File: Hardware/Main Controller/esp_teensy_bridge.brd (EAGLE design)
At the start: 99.8 x 88.1 mm, 64 parts, among them IC1 BQ79600PWRQ1, Q5 VISHAY_SIS862DN-T1-GE3VISHAY_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, Q6 VISHAY_SIS862DN-T1-GE3VISHAY_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, Q7 VISHAY_SIS862DN-T1-GE3VISHAY_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, Q8 VISHAY_SIS862DN-T1-GE3VISHAY_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, X1 5566-12

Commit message: Fixed LED issue
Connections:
- net CONTACTORN_CTRL: now also R14.1
- net CONTACTORPRECHARGE_CTRL: now also R12.1
- net CONTACTORP_CTRL: now also R13.1
- net COOLANT_CTRL: now also R11.1
- net N$12: no longer R12.1
- net N$2: no longer R13.1
- net N$5: no longer R14.1
- net N$6: no longer R11.1
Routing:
- net COOLANT_CTRL: track 36.6 -> 40.7 mm
- net CONTACTORPRECHARGE_CTRL: track 26.1 -> 30.2 mm
- net CONTACTORP_CTRL: track 15.9 -> 19.9 mm
- net CONTACTORN_CTRL: track 11.0 -> 15.0 mm
- net N$6: track 15.3 -> 12.0 mm
- net N$5: track 15.3 -> 12.0 mm
- net N$2: track 16.7 -> 13.4 mm
- net N$12: track 16.7 -> 13.4 mm
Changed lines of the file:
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@@
 <wire x1="9.945" y1="68.58" x2="9.995" y2="68.63" width="0.3048" layer="1"/>
 <wire x1="9.995" y1="68.63" x2="9.995" y2="71.4" width="0.3048" layer="1"/>
+<contactref element="R14" pad="1"/>
+<wire x1="9.1952" y1="71.73125" x2="9.1952" y2="71.9823" width="0.3048" layer="1"/>
+<wire x1="9.1952" y1="71.9823" x2="7.2" y2="73.9775" width="0.3048" layer="1"/>
+<wire x1="9.995" y1="71.4" x2="9.52645" y2="71.4" width="0.3048" layer="1"/>
+<wire x1="9.52645" y1="71.4" x2="9.1952" y2="71.73125" width="0.3048" layer="1"/>
 </signal>
 <signal name="N$5">
 <contactref element="CONTACTOR_N" pad="2"/>
-<contactref element="R14" pad="1"/>
 <contactref element="Q5" pad="5,6,7,8-2"/>
 <contactref element="Q5" pad="5,6,7,8-5"/>
@@
 <wire x1="10.7948" y1="73.5822" x2="10.7948" y2="73.70875" width="0.3048" layer="1"/>
 <wire x1="10.7948" y1="73.70875" x2="10.52605" y2="73.9775" width="0.3048" layer="1"/>
-<wire x1="10.52605" y1="73.9775" x2="7.2" y2="73.9775" width="0.3048" layer="1"/>
 <wire x1="12.98" y1="72.06" x2="12.98" y2="72.72" width="0.3048" layer="1"/>
 <wire x1="11.987" y1="72.39" x2="12.65" y2="72.39" width="0.3048" layer="1"/>
@@
 <signal name="N$2">
 <contactref element="CONTACTOR_P" pad="2"/>
-<contactref element="R13" pad="1"/>
 <contactref element="Q6" pad="5,6,7,8-2"/>
 <contactref element="Q6" pad="5,6,7,8-5"/>
@@
 <wire x1="23.4948" y1="73.5822" x2="23.4948" y2="73.70875" width="0.3048" layer="1"/>
 <wire x1="23.4948" y1="73.70875" x2="23.22605" y2="73.9775" width="0.3048" layer="1"/>
-<wire x1="23.22605" y1="73.9775" x2="19.9" y2="73.9775" width="0.3048" layer="1"/>
 <wire x1="25.68" y1="72.06" x2="25.68" y2="72.72" width="0.3048" layer="1"/>
 <wire x1="25.68" y1="72.06" x2="25.35" y2="72.39" width="0.3048" layer="1"/>
@@
 <wire x1="22.645" y1="68.58" x2="22.695" y2="68.63" width="0.3048" layer="1"/>
 <wire x1="22.695" y1="68.63" x2="22.695" y2="71.4" width="0.3048" layer="1"/>
+<contactref element="R13" pad="1"/>
+<wire x1="21.8952" y1="71.73125" x2="21.8952" y2="71.9823" width="0.3048" layer="1"/>
+<wire x1="21.8952" y1="71.9823" x2="19.9" y2="73.9775" width="0.3048" layer="1"/>
+<wire x1="22.695" y1="71.4" x2="22.22645" y2="71.4" width="0.3048" layer="1"/>
+<wire x1="22.22645" y1="71.4" x2="21.8952" y2="71.73125" width="0.3048" layer="1"/>
 </signal>
 <signal name="CONTACTORPRECHARGE_CTRL">
@@
 <wire x1="35.345" y1="68.58" x2="25.82605" y2="68.58" width="0.3048" layer="1"/>
 <contactref element="Q7" pad="4"/>
-<wire x1="35.345" y1="68.58" x2="35.345" y2="71.35" width="0.3048" layer="1"/>
+<wire x1="35.345" y1="68.58" x2="35.345" y2="71.12" width="0.3048" layer="1"/>
+<wire x1="35.345" y1="71.12" x2="35.345" y2="71.35" width="0.3048" layer="1"/>
 <wire x1="35.345" y1="71.35" x2="35.395" y2="71.4" width="0.3048" layer="1"/>
+<contactref element="R12" pad="1"/>
+<wire x1="32.6" y1="73.9775" x2="34.5952" y2="71.9823" width="0.3048" layer="1"/>
+<wire x1="34.5952" y1="71.9823" x2="34.5952" y2="71.73125" width="0.3048" layer="1"/>
+<wire x1="34.5952" y1="71.73125" x2="34.77375" y2="71.5527" width="0.3048" layer="1"/>
+<wire x1="34.77375" y1="71.5527" x2="34.9123" y2="71.5527" width="0.3048" layer="1"/>
+<wire x1="34.9123" y1="71.5527" x2="35.345" y2="71.12" width="0.3048" layer="1"/>
 </signal>
 <signal name="N$12">
 <contactref element="CONTACTOR_PRECHARGE" pad="2"/>
-<contactref element="R12" pad="1"/>
 <contactref element="Q7" pad="5,6,7,8-2"/>
 <contactref element="Q7" pad="5,6,7,8-5"/>
@@
 <wire x1="36.1948" y1="73.5822" x2="36.1948" y2="73.70875" width="0.3048" layer="1"/>
 <wire x1="36.1948" y1="73.70875" x2="35.92605" y2="73.9775" width="0.3048" layer="1"/>
-<wire x1="35.92605" y1="73.9775" x2="32.6" y2="73.9775" width="0.3048" layer="1"/>
 <wire x1="38.38" y1="72.06" x2="38.05" y2="72.39" width="0.3048" layer="1"/>
 <wire x1="38.05" y1="72.39" x2="37.387" y2="72.39" width="0.3048" layer="1"/>
@@
 <signal name="N$6">
 <contactref element="COOLANT-1" pad="2"/>
-<contactref element="R11" pad="1"/>
 <contactref element="Q8" pad="5,6,7,8-2"/>
 <contactref element="Q8" pad="5,6,7,8-5"/>
@@
 <wire x1="48.8948" y1="73.5822" x2="48.8948" y2="73.70875" width="0.3048" layer="1"/>
 <wire x1="48.8948" y1="73.70875" x2="48.62605" y2="73.9775" width="0.3048" layer="1"/>
-<wire x1="48.62605" y1="73.9775" x2="45.3" y2="73.9775" width="0.3048" layer="1"/>
 <wire x1="51.08" y1="72.06" x2="51.08" y2="72.72" width="0.3048" layer="1"/>
 <wire x1="51.08" y1="72.06" x2="50.75" y2="72.39" width="0.3048" layer="1"/>
@@
 <contactref element="Q8" pad="4"/>
 <wire x1="48.045" y1="68.58" x2="48.095" y2="68.63" width="0.3048" layer="1"/>
-<wire x1="48.095" y1="68.63" x2="48.095" y2="71.4" width="0.3048" layer="1"/>
+<wire x1="48.095" y1="68.63" x2="48.095" y2="71.12" width="0.3048" layer="1"/>
+<contactref element="R11" pad="1"/>
+<wire x1="48.095" y1="71.12" x2="48.095" y2="71.4" width="0.3048" layer="1"/>
+<wire x1="45.3" y1="73.9775" x2="47.2952" y2="71.9823" width="0.3048" layer="1"/>
+<wire x1="47.2952" y1="71.9823" x2="47.2952" y2="71.73125" width="0.3048" layer="1"/>
+<wire x1="47.2952" y1="71.73125" x2="47.47375" y2="71.5527" width="0.3048" layer="1"/>
+<wire x1="47.47375" y1="71.5527" x2="47.6623" y2="71.5527" width="0.3048" layer="1"/>
+<wire x1="47.6623" y1="71.5527" x2="48.095" y2="71.12" width="0.3048" layer="1"/>
 </signal>
 <signal name="N$7">

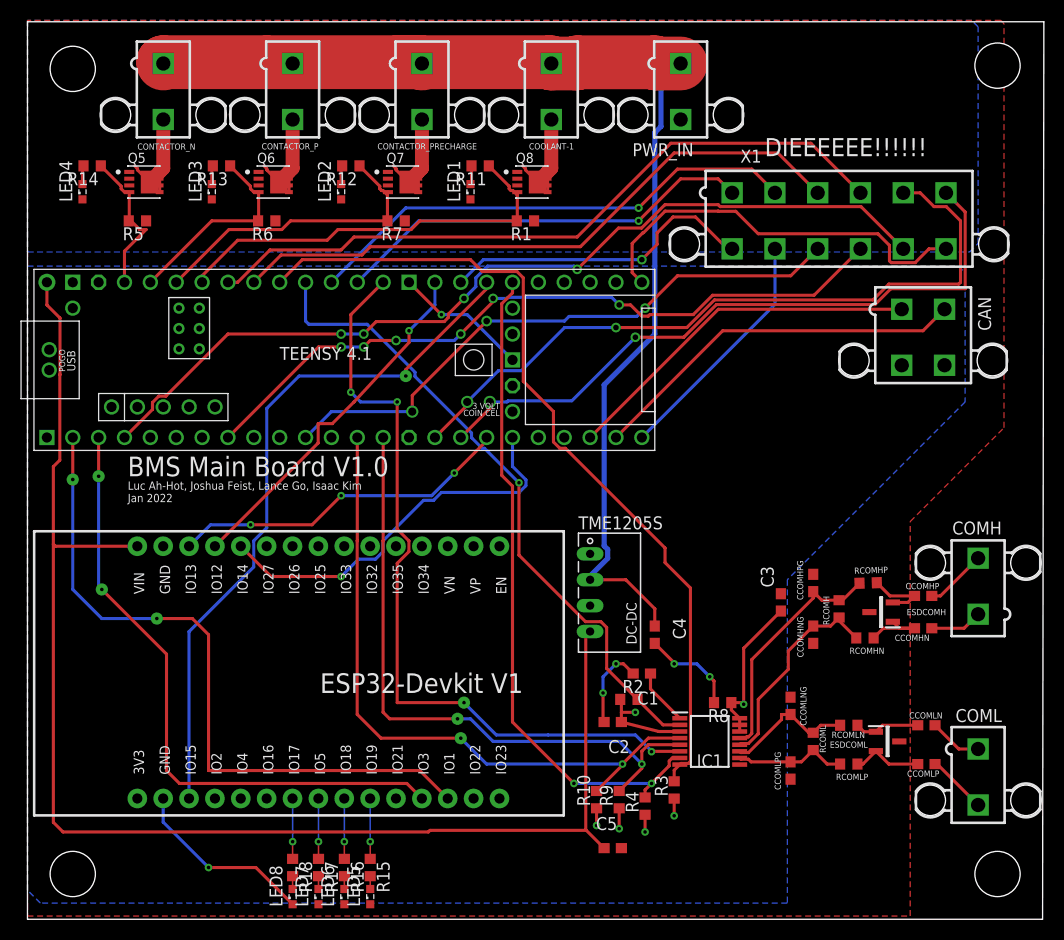
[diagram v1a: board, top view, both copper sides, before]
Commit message: Fixed LED VCC and resistors, coolant is now PWM, CAN transceiver added, removed unnecessary resistor
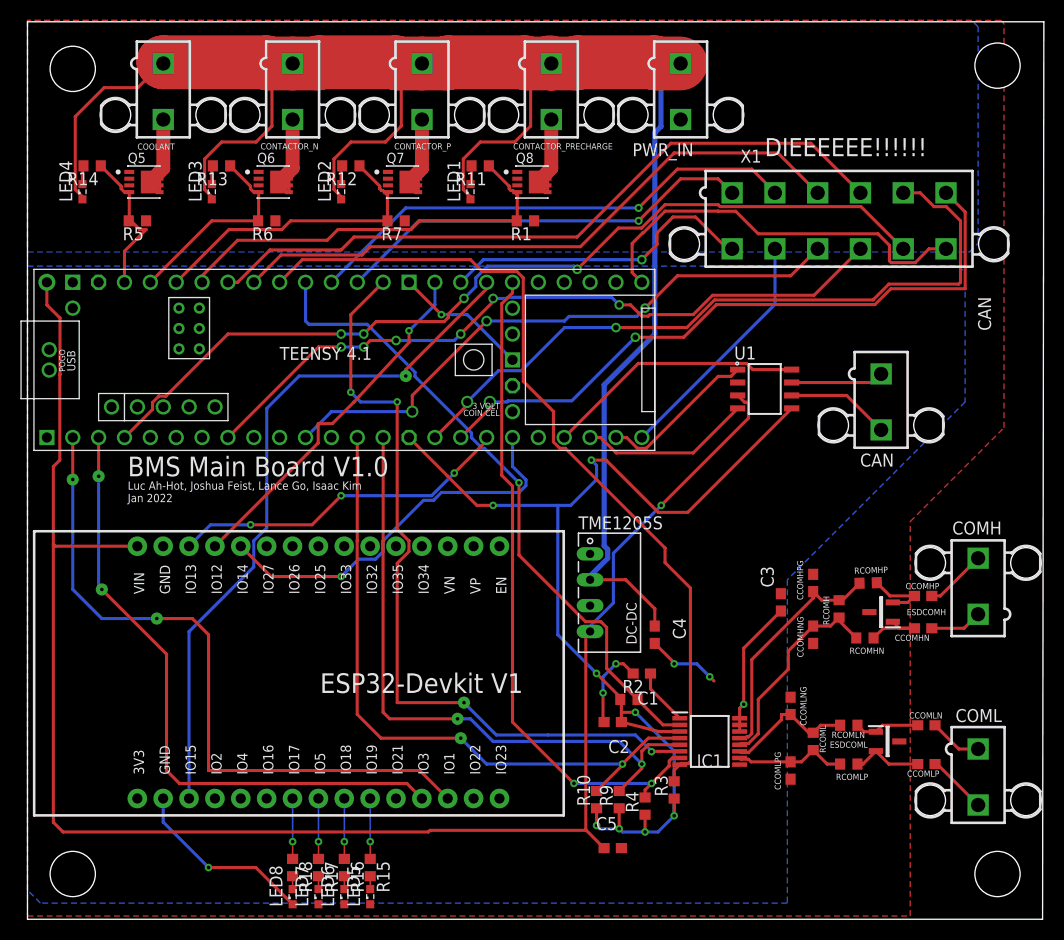
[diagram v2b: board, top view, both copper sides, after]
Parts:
- removed CAN1: 5566-4, con-molex:5566-4
- removed COOLANT-1: 5566-2, con-molex:5566-2
- removed R8: 100k, rcl:R0603
- added CAN, COOLANT: 5566-2, con-molex:5566-2
- added U1: MCP2562-E/SN, MCP2562-E_SN:SOIC127P600X175-8N
- R11, R12, R13, R14: value 100k -> 10k
- moved CONTACTOR_PRECHARGE 12.7 mm to (51.4, 81.3)
- moved CONTACTOR_N 12.7 mm to (26.0, 81.3)
- moved CONTACTOR_P 12.7 mm to (38.7, 81.3)
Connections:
- removed net N$7: CAN1.1, U$3.30-CRX3
- removed net N$8: CAN1.2, U$3.31-CTX3
- removed net NCS/CS: U$3.10-CS\MQSR
- new net 3V3: C2.1, IC1.3, R10.1, R2.1, R3.1, R4.1, R9.1, U$3.3V3-1, U1.5
- new net CANH: CAN.1, U1.7
- new net CANL: CAN.2, U1.6
- new net CRX: U$3.30-CRX3, U1.4
- new net CSTBY: U$3.29-TX7, U1.8
- new net CTX: U$3.31-CTX3, U1.1
- net 5V: now also U1.3; no longer C2.1, IC1.3, R10.1, R2.1, R3.1, R4.1, R8.1, R9.1
- net CONTACTORN_CTRL: now also Q6.4, R13.1, R6.2, U$3.22-A8/CTX1; no longer Q5.4, R14.1, R5.2, U$3.23-A9/CRX1/MCLK1
- net CONTACTORPRECHARGE_CTRL: now also Q8.4, R1.2, R11.1, U$3.20-A6/TX5/LRCLK1; no longer Q7.4, R12.1, R7.2, U$3.21-A7/RX5/BCLK1
- net CONTACTORP_CTRL: now also Q7.4, R12.1, R7.2, U$3.21-A7/RX5/BCLK1; no longer Q6.4, R13.1, R6.2, U$3.22-A8/CTX1
- net COOLANT_CTRL: now also Q5.4, R14.1, R5.2, U$3.23-A9/CRX1/MCLK1; no longer Q8.4, R1.2, R11.1, U$3.20-A6/TX5/LRCLK1
- net GND: now also U1.2; no longer CAN1.3, LED1.C, LED2.C, LED3.C, LED4.C, R8.2
- net N$12: now also CONTACTOR_P.2; no longer CONTACTOR_PRECHARGE.2
- net N$2: now also CONTACTOR_N.2; no longer CONTACTOR_P.2
- net N$5: now also COOLANT.2; no longer CONTACTOR_N.2
- net N$6: now also CONTACTOR_PRECHARGE.2; no longer COOLANT-1.2
- net VCC: now also COOLANT.1, LED1.C, LED2.C, LED3.C, LED4.C; no longer COOLANT-1.1
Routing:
- net 3V3: track 0.00 -> 108.8 mm, vias 0 -> 8
- net VCC: track 117.2 -> 192.1 mm
- net N$8: track 37.5 -> 0.00 mm
- net N$7: track 35.8 -> 0.00 mm
- net COOLANT_CTRL: track 40.7 -> 15.0 mm
- net CSTBY: track 0.00 -> 25.6 mm
- net CRX: track 0.00 -> 16.9 mm
- net CTX: track 0.00 -> 15.6 mm
- net 5V: track 168.8 -> 180.8 mm, vias 6 -> 2
- net CONTACTORPRECHARGE_CTRL: track 30.2 -> 40.7 mm
- net CONTACTORP_CTRL: track 19.9 -> 30.2 mm
- net CANL: track 0.00 -> 10.2 mm
- net CANH: track 0.00 -> 9.13 mm
- net CONTACTORN_CTRL: track 15.0 -> 19.9 mm
- net N$6: track 12.0 -> 9.81 mm
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
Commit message: Work on BQ library, RC fix for SR
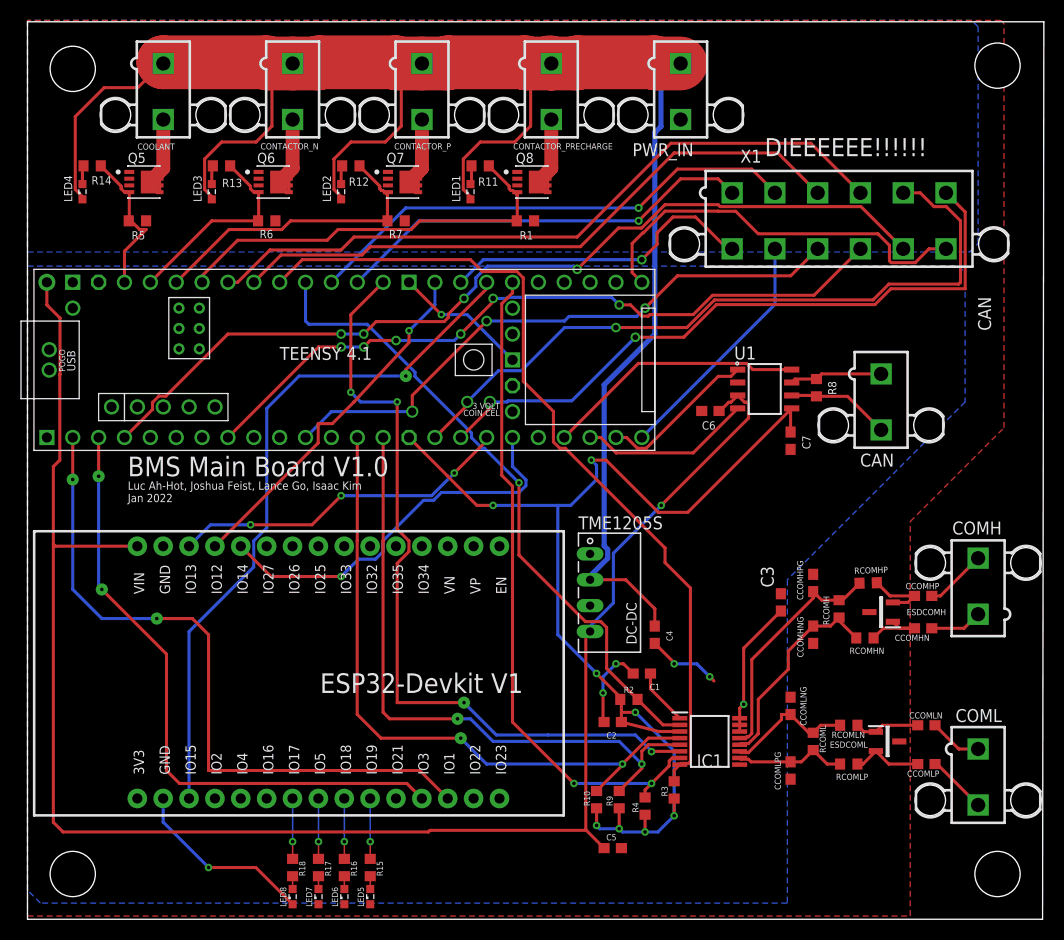
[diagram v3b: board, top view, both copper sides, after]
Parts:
- added C6, C7: 0.1μF, rcl:C0603
- added R8: 120, rcl:R0603
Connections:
- net 3V3: now also C7.1
- net 5V: now also C6.1
- net CANH: now also R8.1
- net CANL: now also R8.2
- net GND: now also C6.2, C7.2
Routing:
- net 5V: track 180.8 -> 183.3 mm
- net 3V3: track 108.8 -> 111.2 mm

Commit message: ESP32-devkitc-32D instead ov DEVKIT V1
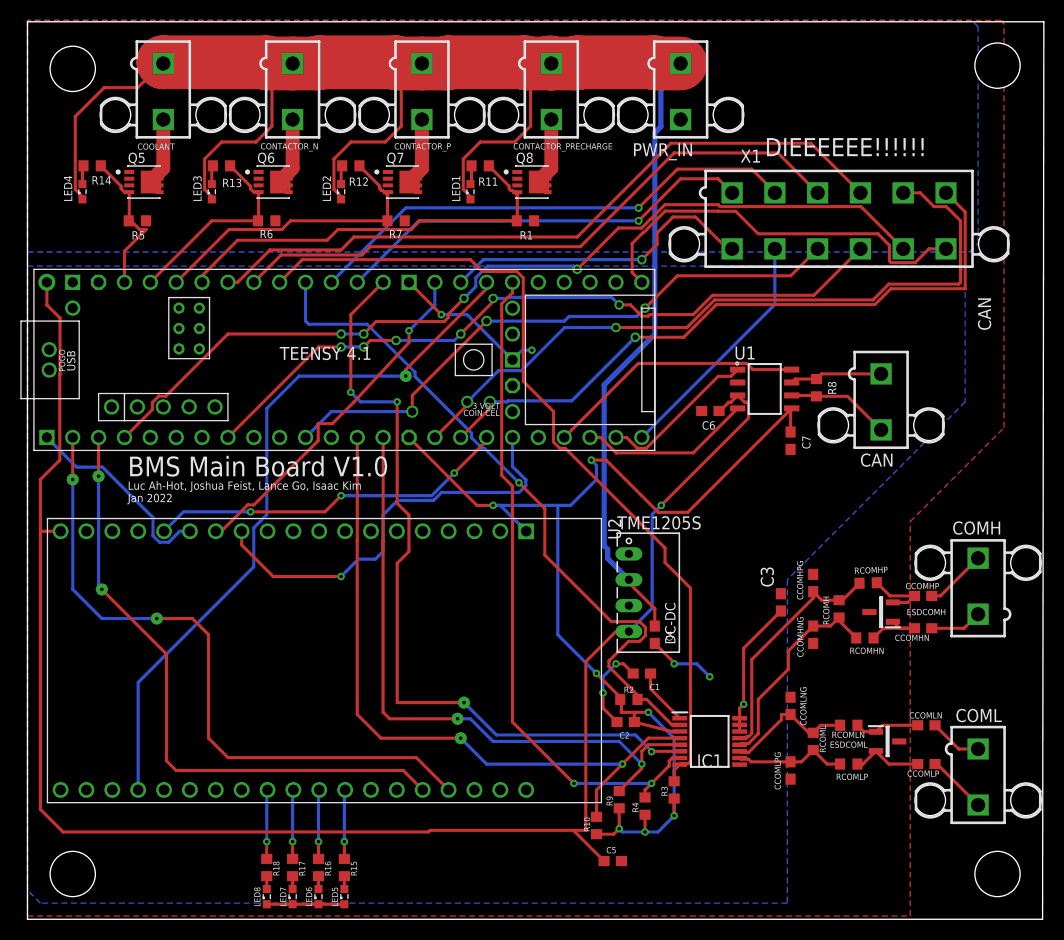
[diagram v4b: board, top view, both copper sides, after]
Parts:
- removed U$2: ESP32DEVKITV1, ESP32-DEVKITV1:ESP32-DEVKITV1
- added U2: ESP32-DEVKITC-32D, ESP32-DEVKITC-32D:MODULE_ESP32-DEVKITC-32D
- moved TME1205S 3.81 mm to (59.1, 32.1)
- moved LED5 2.54 mm to (31.1, 2.22)
- moved R15 2.54 mm to (31.1, 5.08)
- moved R10 2.54 mm to (55.9, 9.21)
- moved LED6 2.54 mm to (28.6, 2.22)
- moved LED7 2.54 mm to (26.0, 2.22)
- moved LED8 2.54 mm to (23.5, 2.22)
- moved R16 2.54 mm to (28.6, 5.08)
- moved R17 2.54 mm to (26.0, 5.08)
- moved R18 2.54 mm to (23.5, 5.08)
- moved C5 1.27 mm to (57.5, 5.71)
- moved C2 1.27 mm to (58.7, 19.4)
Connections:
- new net GND2: U2.26
- new net GND3: U2.20
- net 3V3: now also U2.1
- net 5V: now also U2.19; no longer U$2.30
- net CS1: now also U2.35; no longer U$2.3
- net GND: now also U2.14; no longer U$2.2
- net MISO_ESP: now also U2.13; no longer U$2.27
- net MOSI_ESP: now also U2.15; no longer U$2.28
- net N$28: now also U2.27; no longer U$2.10
- net N$29: now also U2.28; no longer U$2.9
- net N$30: now also U2.29; no longer U$2.8
- net N$31: now also U2.30; no longer U$2.7
- net RX_ESP: now also U2.24; no longer U$2.12
- net SCK_ESP: now also U2.12; no longer U$2.26
- net TX_ESP: now also U2.23; no longer U$2.13
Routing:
- net GND: track 47.5 -> 58.7 mm
- net NFAULT: track 64.0 -> 68.4 mm
- net VCC: track 192.1 -> 188.6 mm
- net SCK_ESP: track 38.8 -> 41.6 mm
- net 5V: track 183.3 -> 180.5 mm
- net MOSI: track 65.6 -> 68.2 mm
- net 3V3: track 111.2 -> 113.4 mm, vias 8 -> 7
- net TX_ESP: track 68.1 -> 65.9 mm
- net MOSI_ESP: track 33.8 -> 35.7 mm
- net CS1: track 68.9 -> 70.2 mm
- net N$28: track 5.93 -> 6.80 mm
- net N$30: track 5.93 -> 6.80 mm
- net N$29: track 5.93 -> 6.80 mm
- net N$31: track 5.93 -> 6.80 mm
- net MISO_ESP: track 35.6 -> 34.7 mm
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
